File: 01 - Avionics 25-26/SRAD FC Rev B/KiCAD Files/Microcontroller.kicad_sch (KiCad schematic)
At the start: 1 part, among them U1 STM32F722RCT6

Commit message: Updated the microcontroller
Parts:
- U1: Link (none) -> https://www.digikey.com/en/products/detail/stmicroelectroni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
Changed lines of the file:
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@@
+			)
+		)
+		(property "Link" "https://www.digikey.com/en/products/detail/stmicroelectronics/STM32F722RCT6/7313338"
+			(at 120.65 93.98 0)
+			(effects
+				(font
+					(size 1.27 1.27)
+				)
+				(hide yes)
 			)
 		)

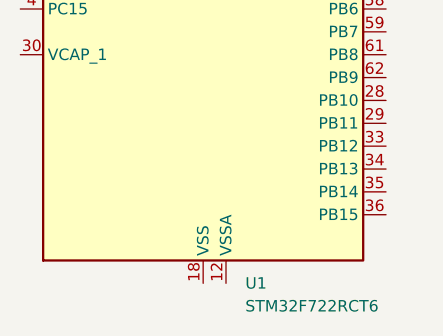
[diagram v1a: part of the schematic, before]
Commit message: Adjusted annotations and named the microcontroller reference
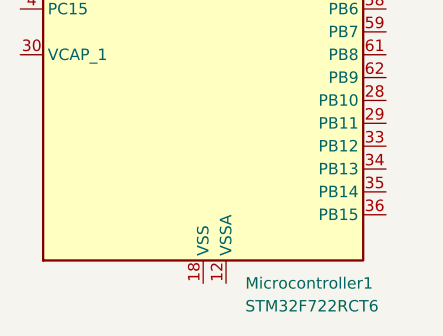
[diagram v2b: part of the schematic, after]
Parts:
- renumbered U1 to Microcontroller1
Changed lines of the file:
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@@
 		(dnp no)
 		(fields_autoplaced yes)
-		(property "Reference" "U1"
+		(property "Reference" "Microcontroller1"
 			(at 125.3333 142.24 0)
 			(effects
@@
 			(project ""
 				(path "/1dd9e63a-24f2-43c6-ae21-66b89e6998f2/9bb21508-08d3-4d29-a04f-971573e7774c"
-					(reference "U1")
+					(reference "Microcontroller1")
 					(unit 1)
 				)

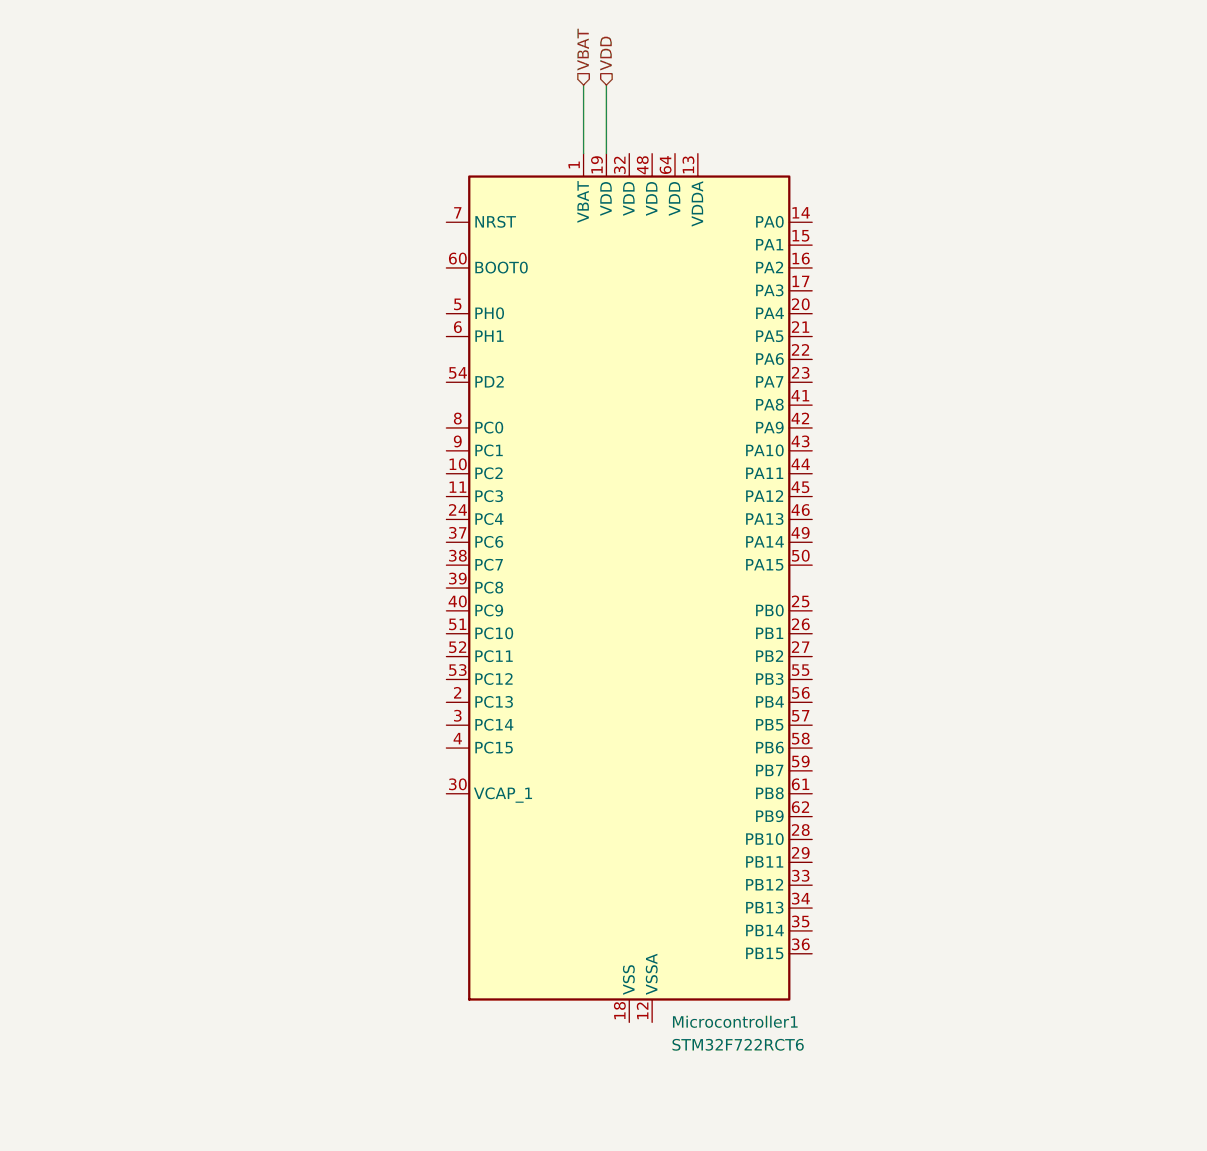
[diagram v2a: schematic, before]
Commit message: made part of the power circuit for the microcontroller
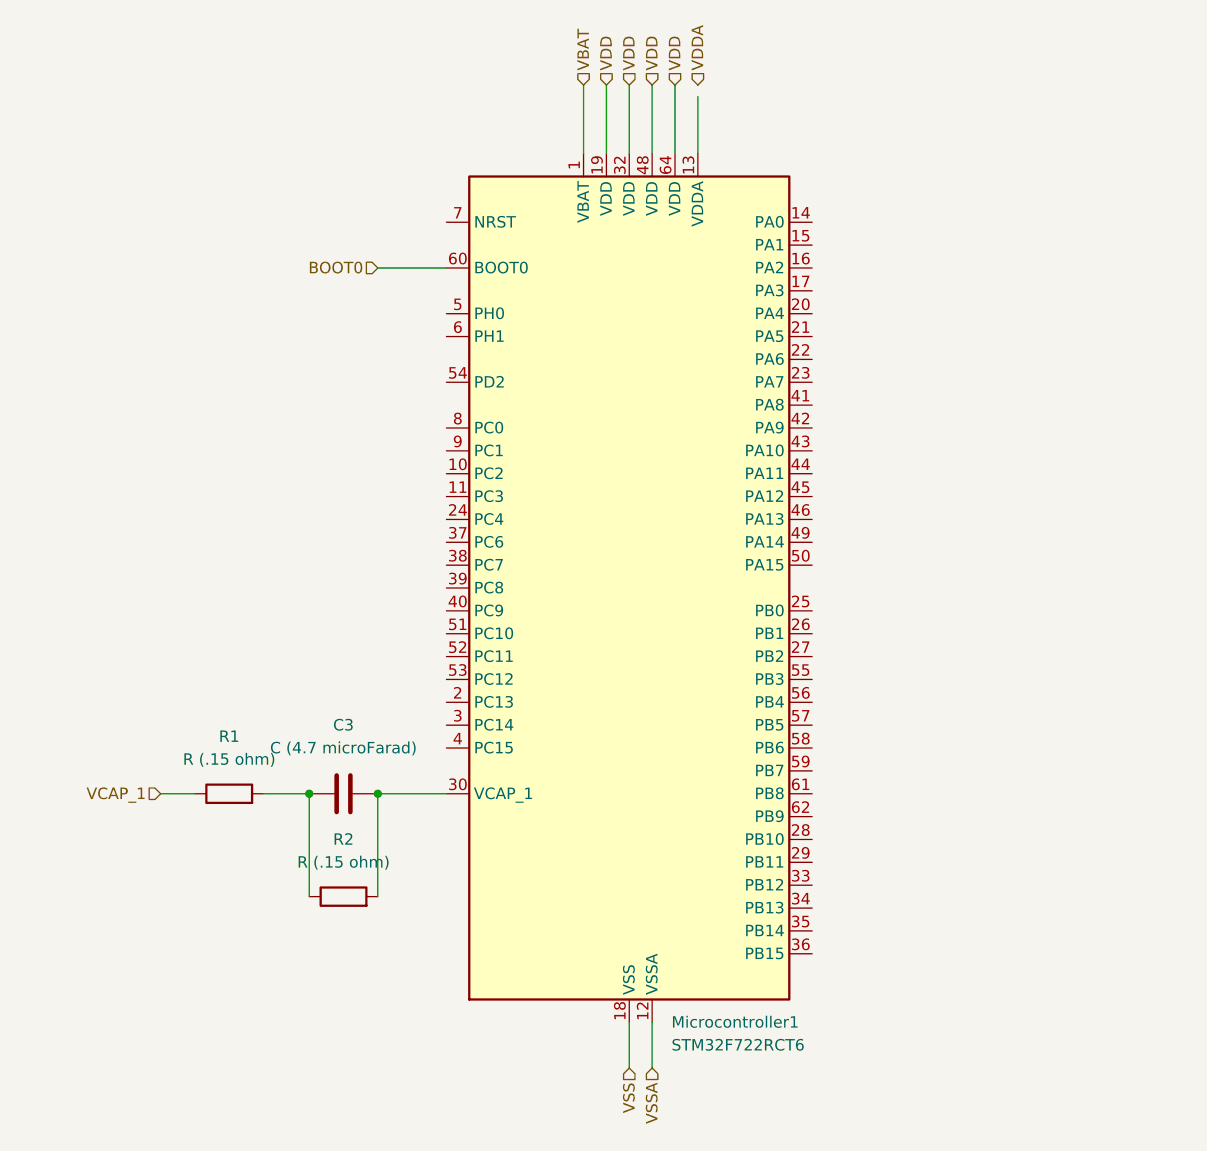
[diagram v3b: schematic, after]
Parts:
- added C3: C (4.7 microFarad), symbol Device:C
- added R1, R2: R (.15 ohm), symbol Device:R
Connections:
- net VDD: now also Microcontroller1.32 (VDD), Microcontroller1.48 (VDD), Microcontroller1.64 (VDD)
- net VSSA: now reaches Microcontroller1.12 (VSSA)
- net VSS: now reaches Microcontroller1.18 (VSS), Microcontroller1.31 (VSS), Microcontroller1.47 (VSS), Microcontroller1.63 (VSS)
- net at Microcontroller1.30 (VCAP_1): now also C3.2, R2.2
- net BOOT0: now reaches Microcontroller1.60 (BOOT0)
- new net: C3.1, R1.2, R2.1
- new net VCAP_1: R1.1

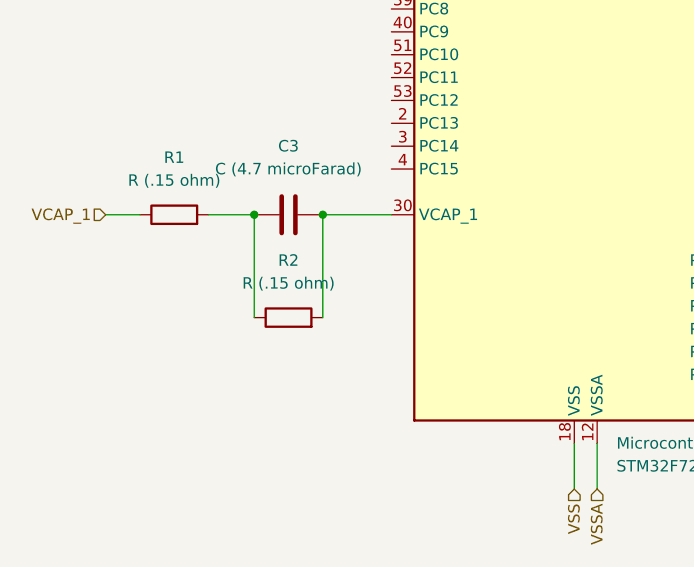
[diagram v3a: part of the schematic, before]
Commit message: Changed a resistor value on the microcontroller draft
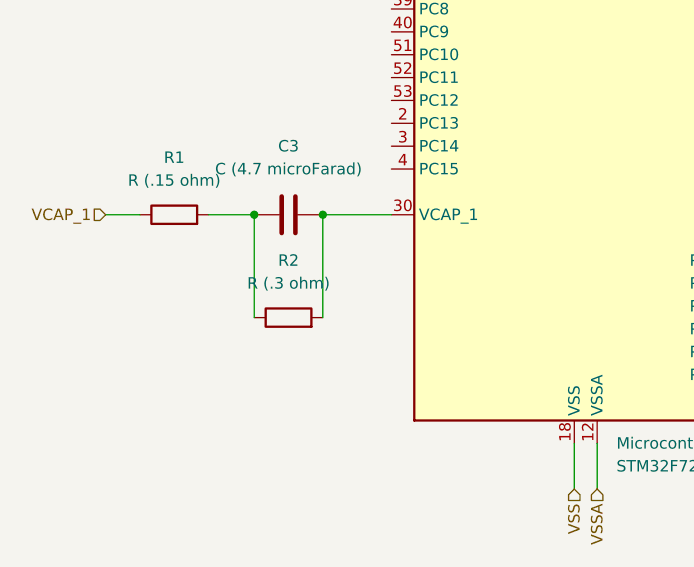
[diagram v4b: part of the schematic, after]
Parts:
- R2: value R (.15 ohm) -> R (.3 ohm)
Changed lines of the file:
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@@
 			)
 		)
-		(property "Value" "R (.15 ohm)"
+		(property "Value" "R (.3 ohm)"
 			(at 88.9 124.46 90)
 			(effects

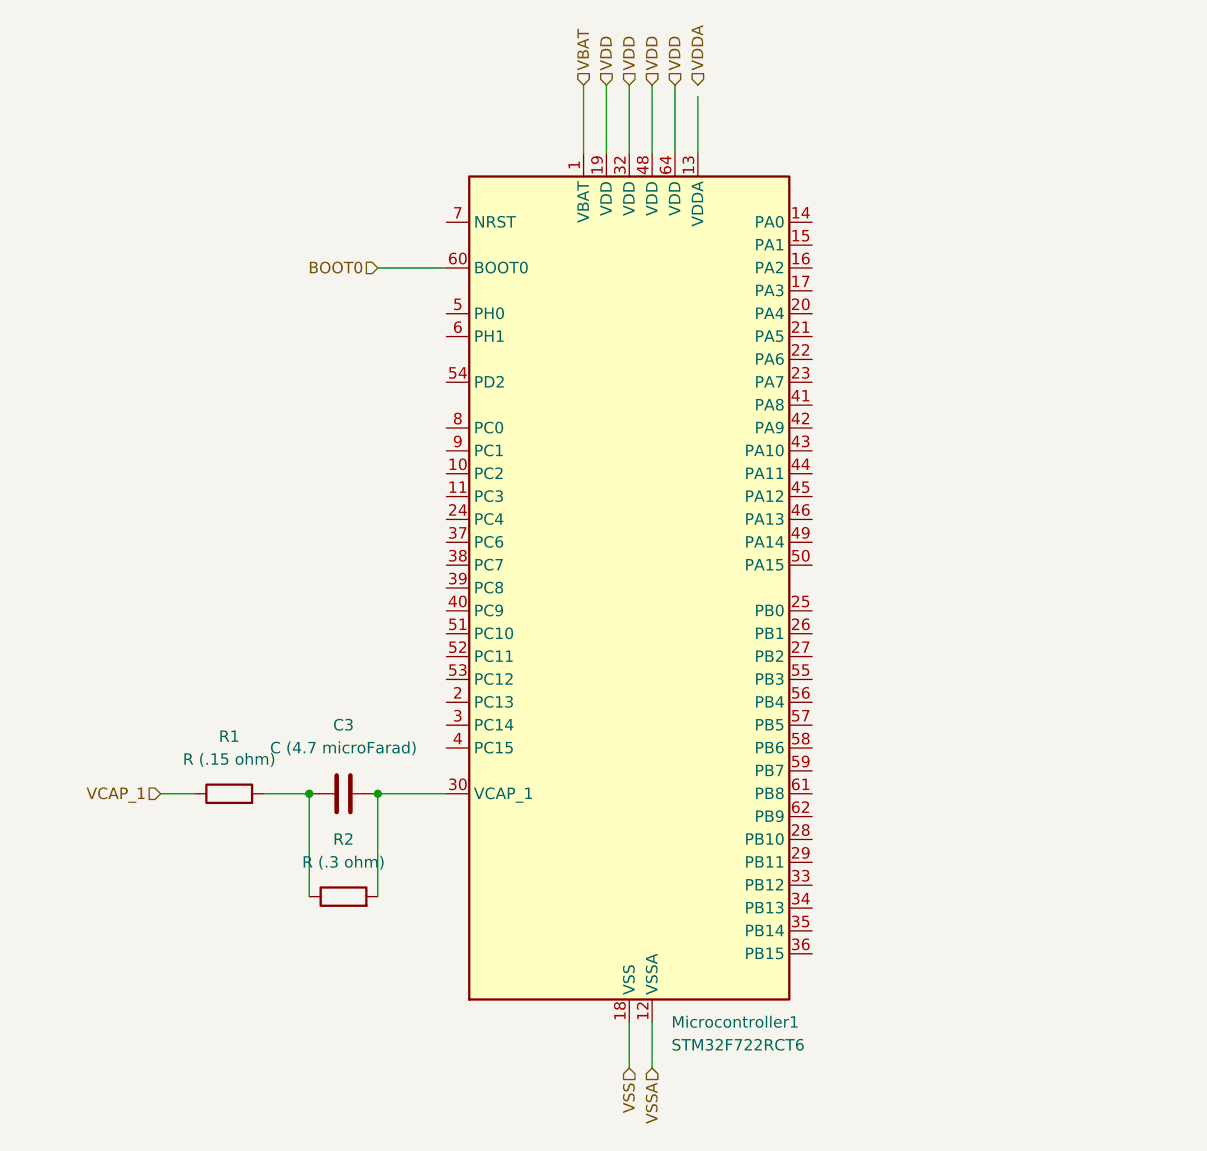
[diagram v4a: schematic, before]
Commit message: added some pins for the MCU related to debugger, also added reset button for MCU
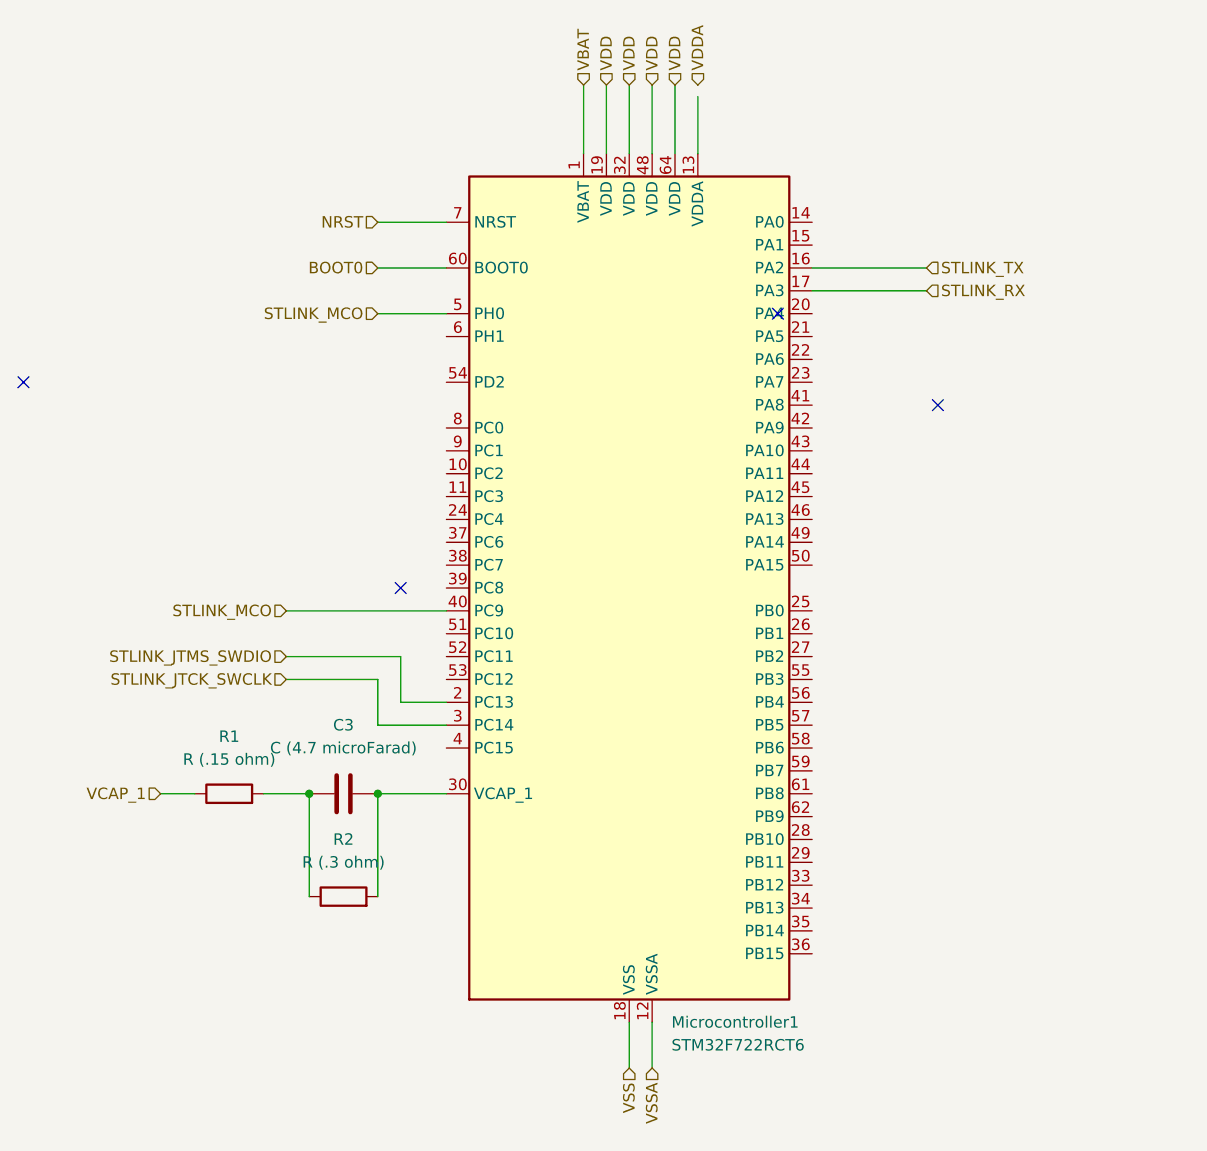
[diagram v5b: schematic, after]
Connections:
- net STLINK_TX: now reaches Microcontroller1.16 (PA2)
- net STLINK_RX: now reaches Microcontroller1.17 (PA3)
- net STLINK_JTMS_SWDIO: now reaches Microcontroller1.2 (PC13)
- net STLINK_JTCK_SWCLK: now reaches Microcontroller1.3 (PC14)
- net STLINK_MCO: now reaches Microcontroller1.40 (PC9)
- net STLINK_MCO: now also Microcontroller1.5 (PH0)
- net NRST: now reaches Microcontroller1.7 (NRST)
- no-connect marks 0 -> 4
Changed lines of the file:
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@@
 		(color 0 0 0 0)
 	)
+	(no_connect
+		(at 154.94 73.66)
+	)
+	(no_connect
+		(at 95.25 93.98)
+	)
+	(no_connect
+		(at 137.16 63.5)
+	)
+	(no_connect
+		(at 53.34 71.12)
+	)
+	(wire
+		(pts
+			(xy 82.55 96.52) (xy 100.33 96.52)
+		)
+		(stroke
+			(width 0)
+			(type default)
+		)
+	)
+	(wire
+		(pts
+			(xy 95.25 101.6) (xy 95.25 106.68)
+		)
+		(stroke
+			(width 0)
+			(type default)
+		)
+	)
 	(wire
 		(pts
@@
 	(wire
 		(pts
+			(xy 140.97 60.96) (xy 153.67 60.96)
+		)
+		(stroke
+			(width 0)
+			(type default)
+		)
+	)
+	(wire
+		(pts
 			(xy 120.65 38.1) (xy 120.65 45.72)
 		)
@@
 	(wire
 		(pts
+			(xy 140.97 58.42) (xy 153.67 58.42)
+		)
+		(stroke
+			(width 0)
+			(type default)
+		)
+	)
+	(wire
+		(pts
+			(xy 95.25 106.68) (xy 100.33 106.68)
+		)
+		(stroke
+			(width 0)
+			(type default)
+		)
+	)
+	(wire
+		(pts
 			(xy 115.57 38.1) (xy 115.57 45.72)
 		)
@@
 	(wire
 		(pts
+			(xy 92.71 104.14) (xy 82.55 104.14)
+		)
+		(stroke
+			(width 0)
+			(type default)
+		)
+	)
+	(wire
+		(pts
 			(xy 125.73 38.1) (xy 125.73 45.72)
 		)
@@
 	(wire
 		(pts
+			(xy 82.55 101.6) (xy 95.25 101.6)
+		)
+		(stroke
+			(width 0)
+			(type default)
+		)
+	)
+	(wire
+		(pts
+			(xy 92.71 53.34) (xy 100.33 53.34)
+		)
+		(stroke
+			(width 0)
+			(type default)
+		)
+	)
+	(wire
+		(pts
 			(xy 92.71 116.84) (xy 92.71 128.27)
 		)
@@
 		)
 	)
+	(wire
+		(pts
+			(xy 92.71 109.22) (xy 92.71 104.14)
+		)
+		(stroke
+			(width 0)
+			(type default)
+		)
+	)
+	(wire
+		(pts
+			(xy 92.71 63.5) (xy 100.33 63.5)
+		)
+		(stroke
+			(width 0)
+			(type default)
+		)
+	)
+	(wire
+		(pts
+			(xy 100.33 109.22) (xy 92.71 109.22)
+		)
+		(stroke
+			(width 0)
+			(type default)
+		)
+	)
 	(hierarchical_label "VDD"
 		(shape input)
@@
 		)
 	)
+	(hierarchical_label "STLINK_JTCK_SWCLK"
+		(shape input)
+		(at 82.55 104.14 180)
+		(effects
+			(font
+				(size 1.27 1.27)
+			)
+			(justify right)
+		)
+	)
 	(hierarchical_label "VCAP_1"
 		(shape input)
@@
 		)
 	)
+	(hierarchical_label "STLINK_RX"
+		(shape input)
+		(at 153.67 60.96 0)
+		(effects
+			(font
+				(size 1.27 1.27)
+			)
+			(justify left)
+		)
+	)
+	(hierarchical_label "STLINK_MCO"
+		(shape input)
+		(at 92.71 63.5 180)
+		(effects
+			(font
+				(size 1.27 1.27)
+			)
+			(justify right)
+		)
+	)
+	(hierarchical_label "STLINK_JTMS_SWDIO"
+		(shape input)
+		(at 82.55 101.6 180)
+		(effects
+			(font
+				(size 1.27 1.27)
+			)
+			(justify right)
+		)
+	)
 	(hierarchical_label "VSSA"
 		(shape input)
@@
 		)
 	)
+	(hierarchical_label "STLINK_TX"
+		(shape input)
+		(at 153.67 58.42 0)
+		(effects
+			(font
+				(size 1.27 1.27)
+			)
+			(justify left)
+		)
+	)
 	(hierarchical_label "VDD"
 		(shape input)
@@
 		)
 	)
+	(hierarchical_label "NRST"
+		(shape input)
+		(at 92.71 53.34 180)
+		(effects
+			(font
+				(size 1.27 1.27)
+			)
+			(justify right)
+		)
+	)
+	(hierarchical_label "STLINK_MCO"
+		(shape input)
+		(at 82.55 96.52 180)
+		(effects
+			(font
+				(size 1.27 1.27)
+			)
+			(justify right)
+		)
+	)
